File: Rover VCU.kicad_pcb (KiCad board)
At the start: 4 copper layers, 86.2 x 39 mm, 97 parts, among them J1 Conn_ST_STDC14, J2 USB4105-GF-A, J3 430450400, J6 430451200, SW1 TS-1088-AR02016, U1 STM32H563RITx, U3 DP83TC812RRHARQ1, U4 SN65HVD230, U5 SN65HVD230, U6 LMR51610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

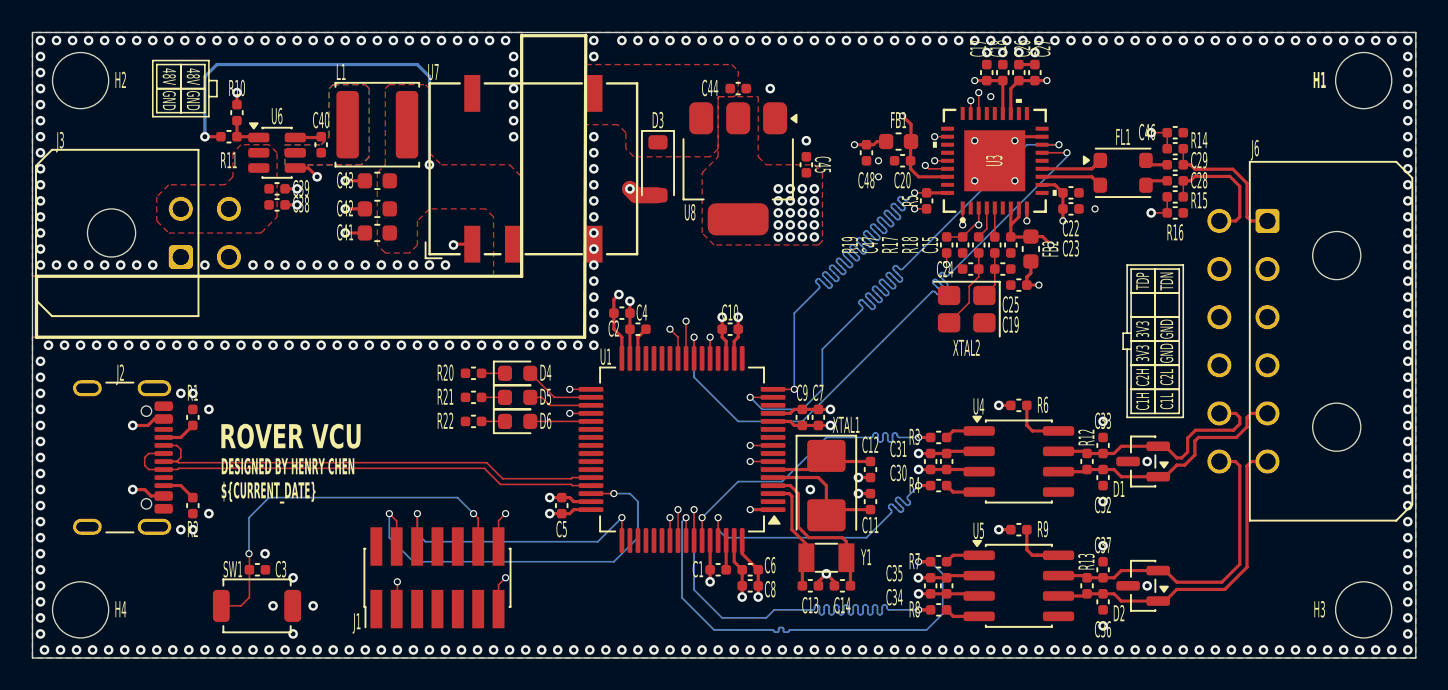
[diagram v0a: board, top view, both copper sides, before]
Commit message: fix: updated 12pin connector footprint + fix drc and exposed vias
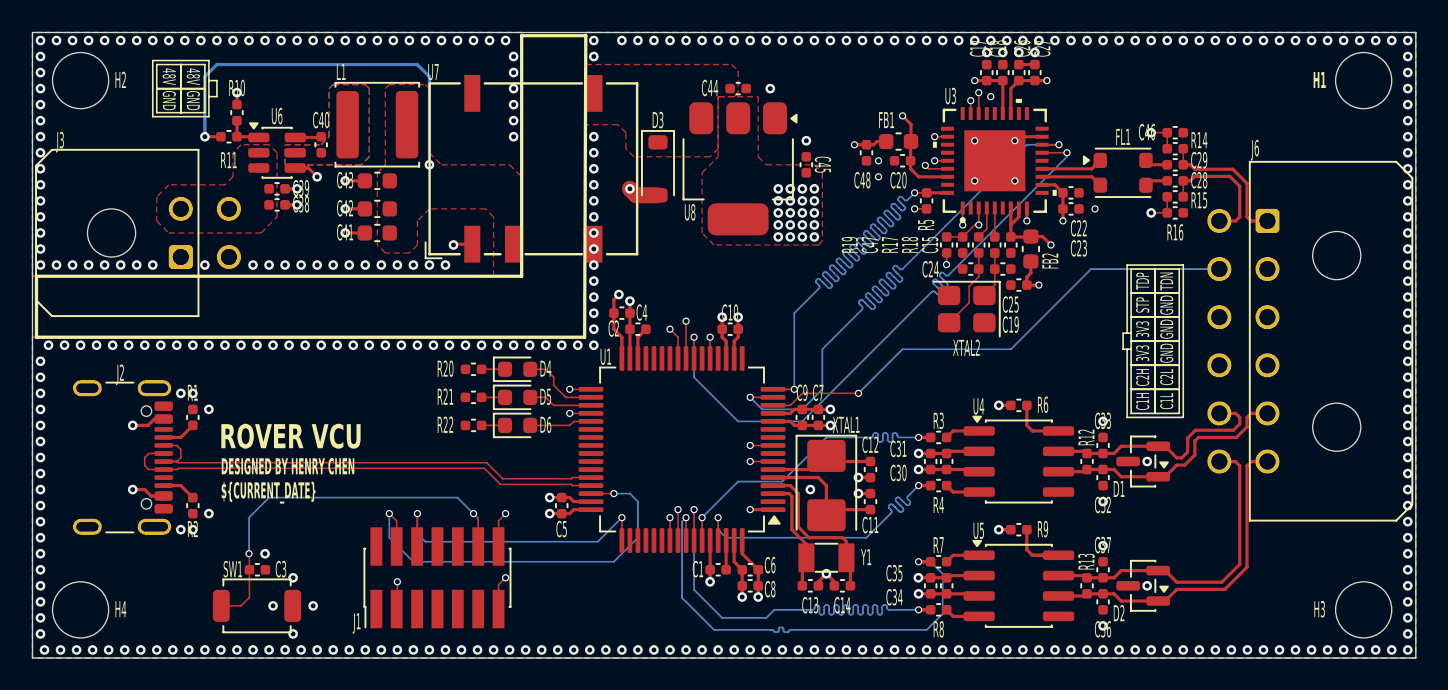
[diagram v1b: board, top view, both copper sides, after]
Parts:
- moved D4 0.25 mm to (133.0, 101.0)
- moved D6 0.25 mm to (133.0, 104.5)
- moved R20 0.25 mm to (130.2, 101.0)
- moved R22 0.25 mm to (130.2, 104.5)
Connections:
- J6 pad 2: unconnected-(J6-Pin_2-Pad2) -> GND
- J6 pad 8: unconnected-(J6-Pin_8-Pad8) -> /ESTOP
- U1 pad 14: unconnected-(U1-PA0-Pad14) -> /ESTOP
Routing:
- net /ESTOP: track 0.00 -> 31.3 mm, vias 0 -> 1
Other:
- board text added: "STP"

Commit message: fix: tiny fixes; adjusted pin names as check
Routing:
- net /MCU/RMII_MDC: track 42.5 -> 43.2 mm

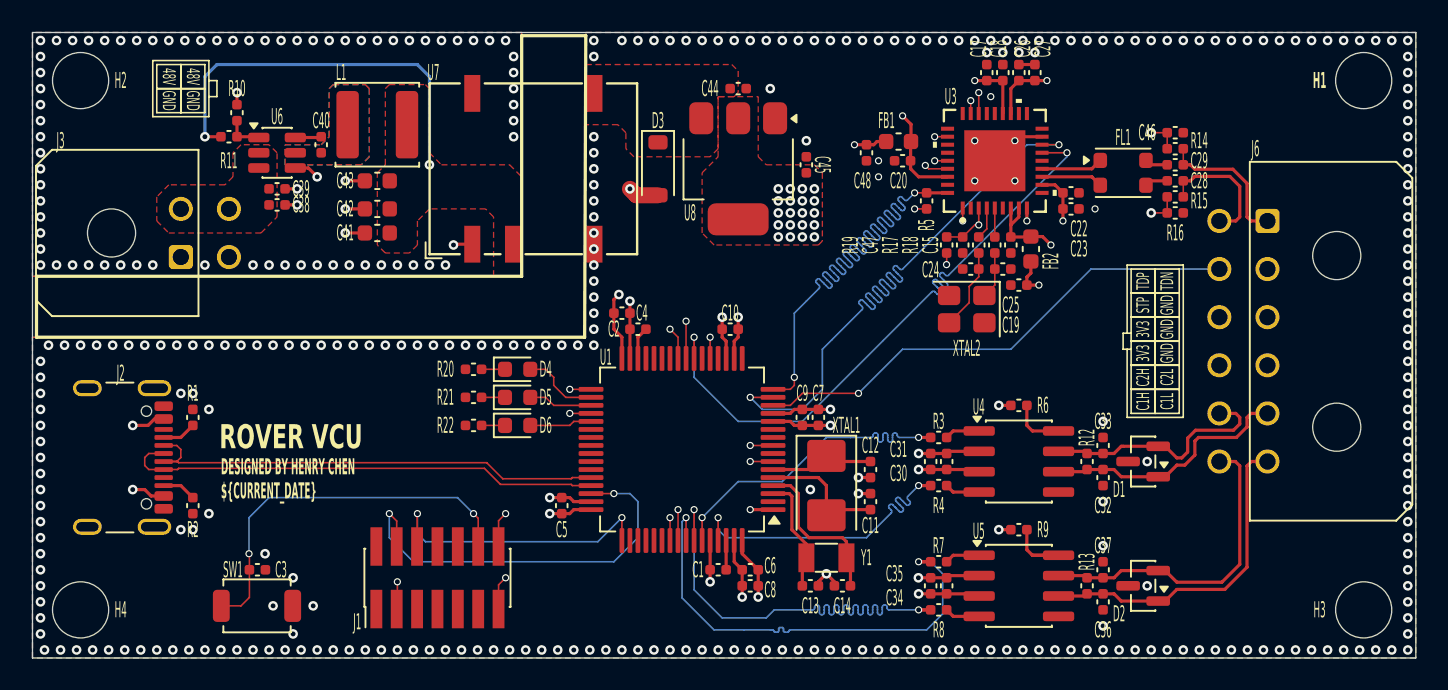
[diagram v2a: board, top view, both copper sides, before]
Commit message: fix: added leds to phy
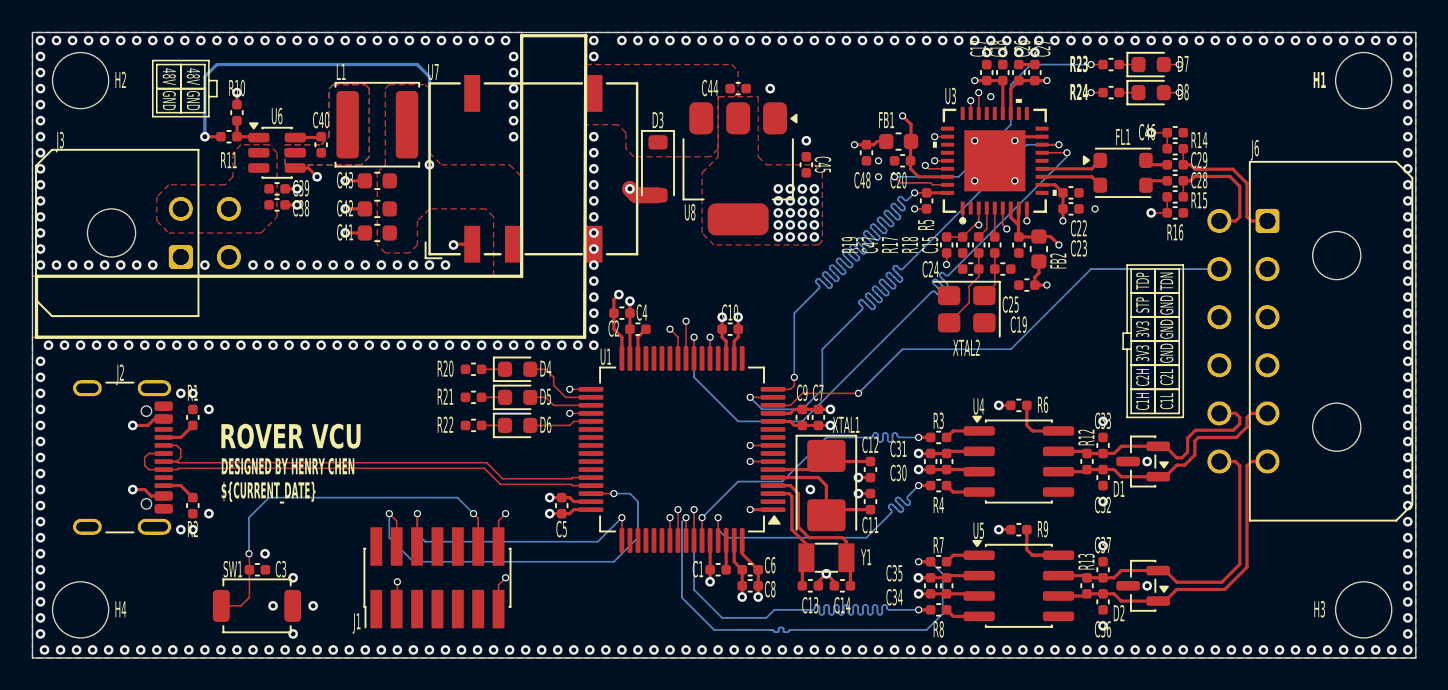
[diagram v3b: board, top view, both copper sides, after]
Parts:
- added D7: LED_RED_0603, LED_SMD:LED_0603_1608Metric, F.Cu at (172.5, 82.0)
- added D8: LED_RED_0603, LED_SMD:LED_0603_1608Metric, F.Cu at (172.5, 83.8)
- added R23: 5K1, chenry-footprint-lib:R_0402, F.Cu at (170.0, 82.0)
- added R24: 5K1, chenry-footprint-lib:R_0402, F.Cu at (170.0, 83.8)
- moved C15 0.50 mm to (164.2, 93.2)
- moved C19 0.50 mm to (164.8, 95.8)
- moved FB2 0.50 mm to (165.5, 93.5)
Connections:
- U3 pad 35: unconnected-(U3-LED_0-Pad35) -> Net-(U3-LED_0)
- U3 pad 6: unconnected-(U3-LED_1-Pad6) -> Net-(U3-LED_1)
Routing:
- net Net-(U3-LED_0): track 0.00 -> 20.9 mm, vias 0 -> 2
- net Net-(U3-LED_1): track 0.00 -> 15.4 mm, vias 0 -> 2
- net /VDD_3V3: track 34.0 -> 35.9 mm, vias 33 -> 35
- net Net-(D8-K): track 0.00 -> 1.21 mm
- net Net-(D7-K): track 0.00 -> 1.21 mm
